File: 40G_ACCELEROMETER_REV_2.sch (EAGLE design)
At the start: 25 parts, among them IC1 3.3V_LDO, IC2 X_BUFFER, IC3 Y_BUFFER, IC4 Z_BUFFER

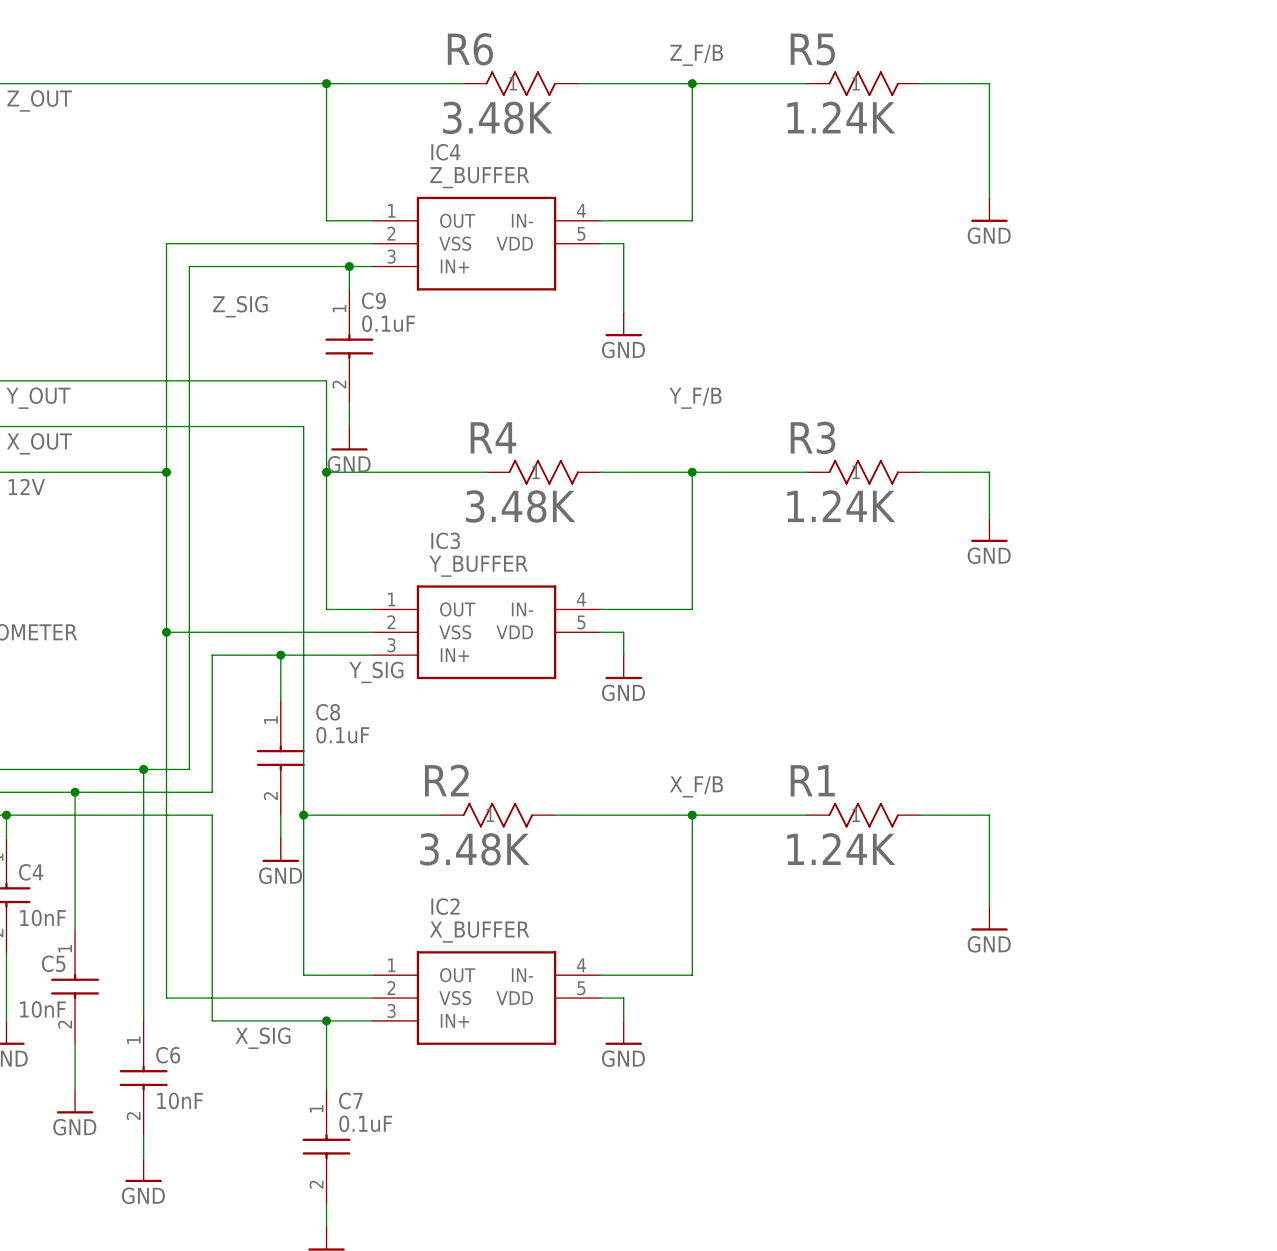
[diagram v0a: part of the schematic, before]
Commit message: New revision of board layout and fixed power connections to buffers in schematic.
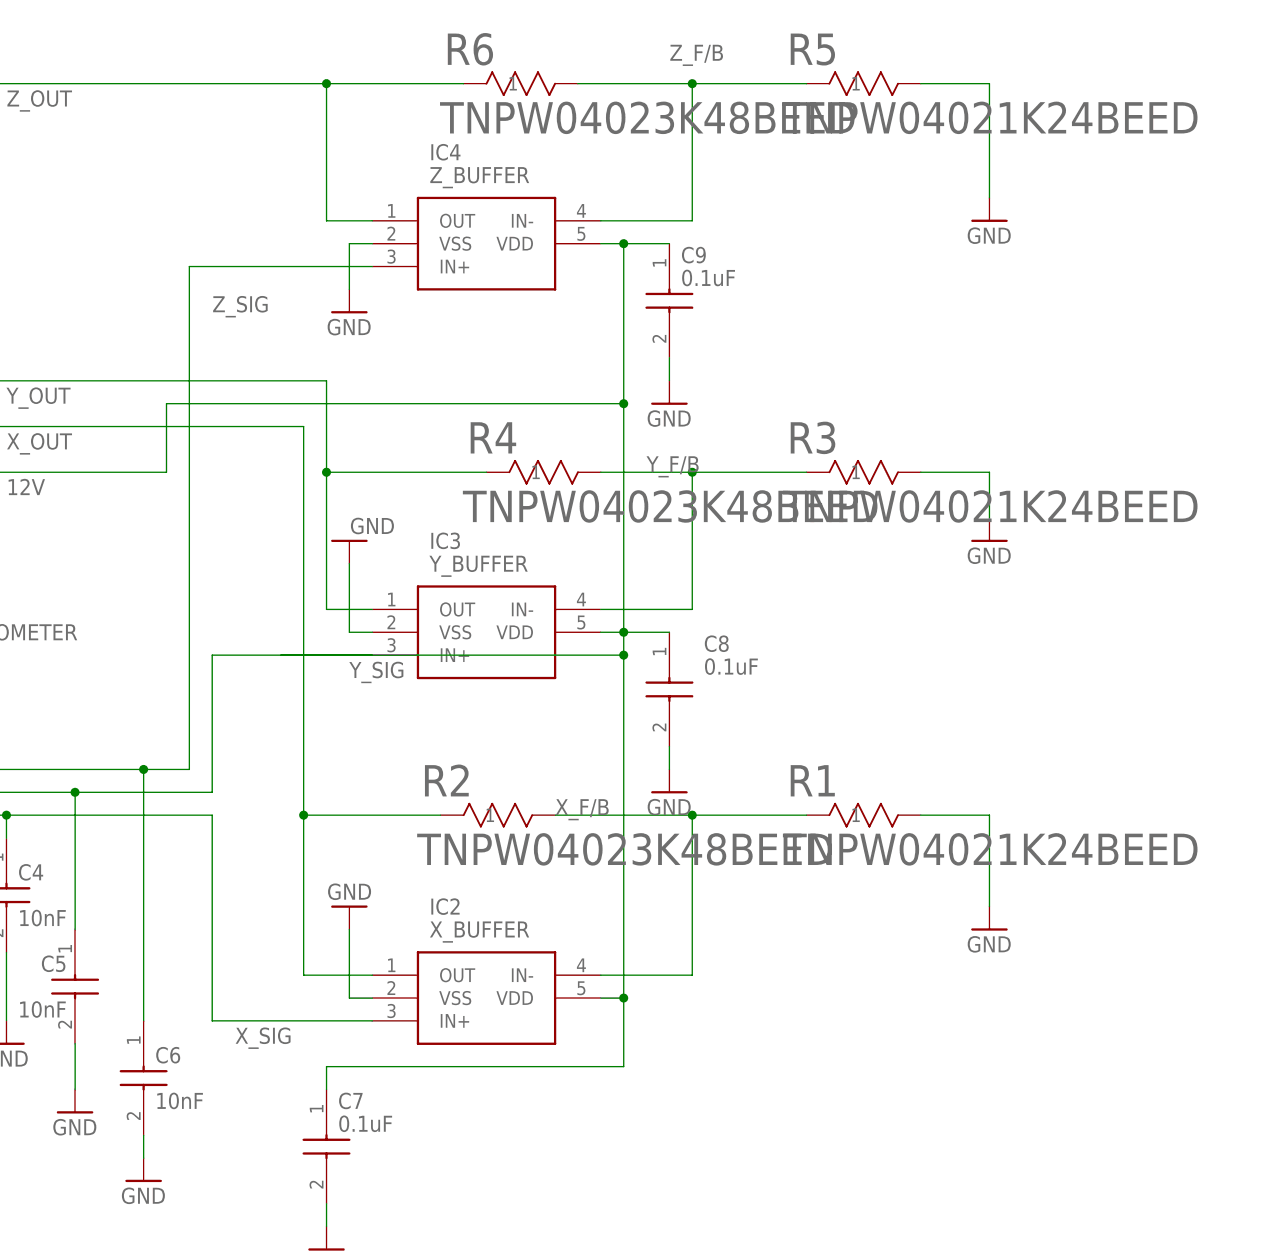
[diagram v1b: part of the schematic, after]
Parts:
- R1, R3, R5: value 1.24K -> TNPW04021K24BEED
- R2, R4, R6: value 3.48K -> TNPW04023K48BEED
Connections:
- net 12V: now also C7.1, C8.1, C9.1, IC2.VDD, IC3.VDD, IC4.VDD; no longer IC2.VSS, IC3.VSS, IC4.VSS
- net GND: now also IC2.VSS, IC3.VSS, IC4.VSS; no longer IC2.VDD, IC3.VDD, IC4.VDD
- net X_SIG: no longer C7.1
- net Y_SIG: no longer C8.1
- net Z_SIG: no longer C9.1
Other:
- moved on the sheet: C8, C9

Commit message: New layout for PCB board. Added diodes to main board pins. Ground stitching vias added. Ready for final review.
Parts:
- added D1, D2, D3, D4, D5: PTVS12VS1UR,115, SamacSys_Parts:PTVS12VS1UR,115
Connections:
- net 12V: now also D1.K
- net GND: now also D1.A, D2.A, D3.A, D4.A, D5.A, D5.K
- net X_OUT: now also D2.K
- net Y_OUT: now also D3.K
- net Z_OUT: now also D4.K
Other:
- moved on the sheet: 12V, C8, C9, GND, R1, R2, X_OUT, Y_OUT, Z_OUT

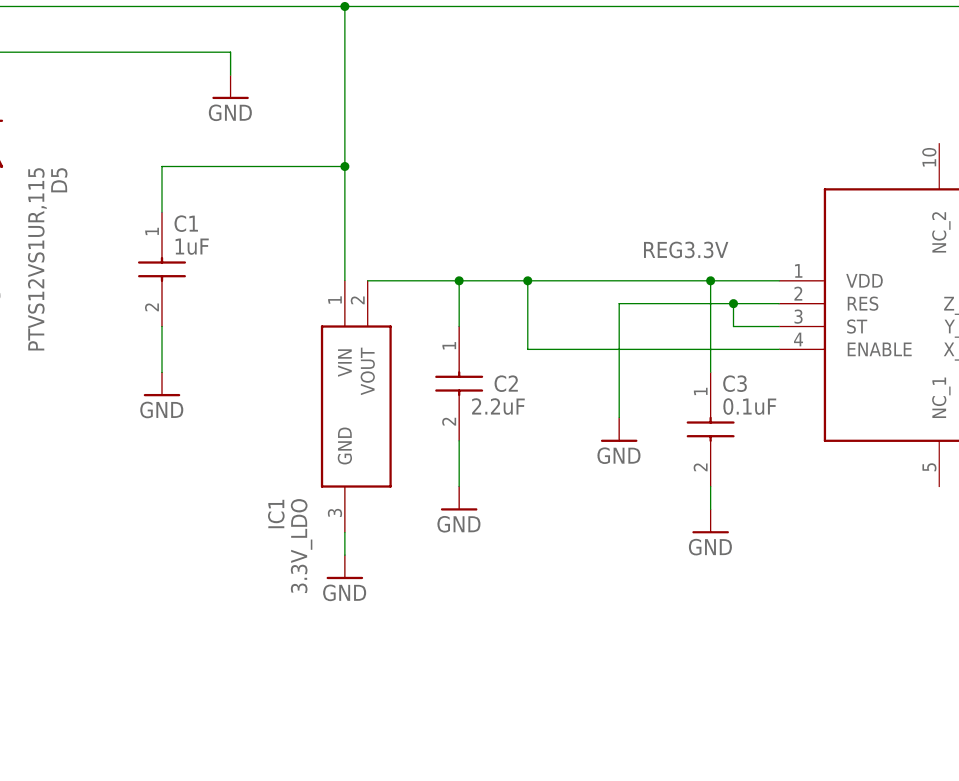
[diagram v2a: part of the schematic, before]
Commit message: Changed LDO input cap and LDO to parts that are in stock.
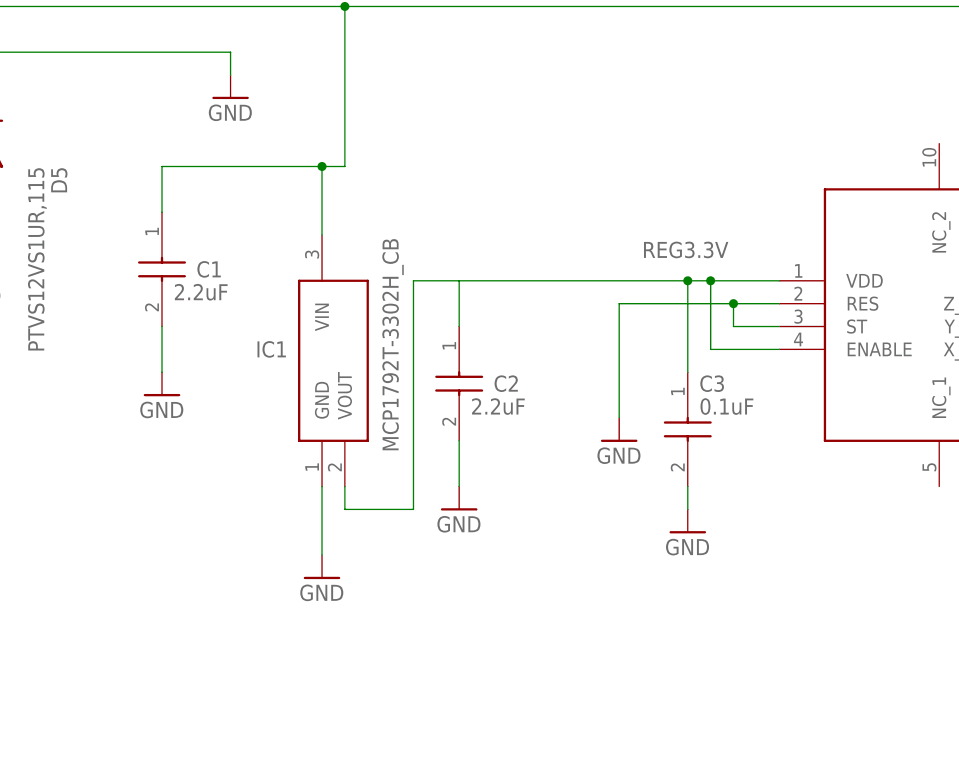
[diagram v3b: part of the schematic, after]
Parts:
- C1: value 1uF -> 2.2uF; device SamacSys_Parts:CGA3E1X7R1V105K080AE -> SamacSys_Parts:CGA3E1X7R0J225K080AC
- IC1: value 3.3V_LDO -> MCP1792T-3302H_CB; device SamacSys_Parts:AP7384-33SA-7 -> SamacSys_Parts:MCP1792T-3302H_CB
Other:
- moved on the sheet: C3, IC1
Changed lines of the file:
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@@
 <parts>
 <part name="AC1" library="SamacSys_Parts" deviceset="KX220-1072" device="" value="ACCELEROMETER"/>
-<part name="IC1" library="SamacSys_Parts" deviceset="AP7384-33SA-7" device="" value="3.3V_LDO"/>
 <part name="IC2" library="SamacSys_Parts" deviceset="NCS21911SN2T1G" device="" value="X_BUFFER"/>
 <part name="IC3" library="SamacSys_Parts" deviceset="NCS21911SN2T1G" device="" value="Y_BUFFER"/>
@@
 <part name="GND9" library="supply1" library_urn="urn:adsk.eagle:library:371" deviceset="GND" device=""/>
 <part name="GND10" library="supply1" library_urn="urn:adsk.eagle:library:371" deviceset="GND" device=""/>
-<part name="C1" library="SamacSys_Parts" deviceset="CGA3E1X7R1V105K080AE" device="" value="1uF"/>
 <part name="GND11" library="supply1" library_urn="urn:adsk.eagle:library:371" deviceset="GND" device=""/>
 <part name="C7" library="SamacSys_Parts" deviceset="CGA3E2X7R1H104K080AE" device="" value="0.1uF"/>
@@
 <part name="GND23" library="supply1" library_urn="urn:adsk.eagle:library:371" deviceset="GND" device=""/>
 <part name="GND24" library="supply1" library_urn="urn:adsk.eagle:library:371" deviceset="GND" device=""/>
+<part name="C1" library="SamacSys_Parts" deviceset="CGA3E1X7R0J225K080AC" device="" value="2.2uF"/>
+<part name="IC1" library="SamacSys_Parts" deviceset="MCP1792T-3302H_CB" device=""/>
 </parts>
 <sheets>
@@
 <attribute name="VALUE" x="97.79" y="63.5" size="1.778" layer="96" align="center-left"/>
 </instance>
-<instance part="IC1" gate="G$1" x="17.78" y="50.8" smashed="yes" rot="MR270">
-<attribute name="NAME" x="10.16" y="26.67" size="1.778" layer="95" rot="MR270" align="center-left"/>
-<attribute name="VALUE" x="12.7" y="26.67" size="1.778" layer="96" rot="MR270" align="center-left"/>
-</instance>
 <instance part="IC2" gate="G$1" x="149.86" y="25.4" smashed="yes">
 <attribute name="NAME" x="156.21" y="33.02" size="1.778" layer="95" align="center-left"/>
@@
 <attribute name="VALUE" x="215.9" y="27.94" size="1.778" layer="96"/>
 </instance>
-<instance part="GND6" gate="1" x="17.78" y="17.78" smashed="yes">
-<attribute name="VALUE" x="15.24" y="15.24" size="1.778" layer="96"/>
+<instance part="GND6" gate="1" x="15.24" y="17.78" smashed="yes">
+<attribute name="VALUE" x="12.7" y="15.24" size="1.778" layer="96"/>
 </instance>
 <instance part="C2" gate="G$1" x="30.48" y="45.72" smashed="yes" rot="R270">
@@
 <attribute name="VALUE" x="121.92" y="0" size="1.778" layer="96"/>
 </instance>
-<instance part="C1" gate="G$1" x="-2.54" y="58.42" smashed="yes" rot="R270">
-<attribute name="NAME" x="-1.27" y="57.15" size="1.778" layer="95" align="center-left"/>
-<attribute name="VALUE" x="-1.27" y="54.61" size="1.778" layer="96" align="center-left"/>
-</instance>
 <instance part="GND11" gate="1" x="-2.54" y="38.1" smashed="yes">
 <attribute name="VALUE" x="-5.08" y="35.56" size="1.778" layer="96"/>
@@
 <attribute name="VALUE" x="142.24" y="-7.62" size="1.778" layer="96"/>
 </instance>
-<instance part="C3" gate="G$1" x="58.42" y="40.64" smashed="yes" rot="R270">
-<attribute name="NAME" x="59.69" y="39.37" size="1.778" layer="95" align="center-left"/>
-<attribute name="VALUE" x="59.69" y="36.83" size="1.778" layer="96" align="center-left"/>
-</instance>
-<instance part="GND18" gate="1" x="58.42" y="22.86" smashed="yes">
-<attribute name="VALUE" x="55.88" y="20.32" size="1.778" layer="96"/>
+<instance part="C3" gate="G$1" x="55.88" y="40.64" smashed="yes" rot="R270">
+<attribute name="NAME" x="57.15" y="39.37" size="1.778" layer="95" align="center-left"/>
+<attribute name="VALUE" x="57.15" y="36.83" size="1.778" layer="96" align="center-left"/>
+</instance>
+<instance part="GND18" gate="1" x="55.88" y="22.86" smashed="yes">
+<attribute name="VALUE" x="53.34" y="20.32" size="1.778" layer="96"/>
 </instance>
 <instance part="GND19" gate="1" x="5.08" y="71.12" smashed="yes">
@@
 <attribute name="VALUE" x="-25.4" y="48.26" size="1.778" layer="96"/>
 </instance>
+<instance part="C1" gate="G$1" x="-2.54" y="58.42" smashed="yes" rot="R270">
+<attribute name="NAME" x="1.27" y="52.07" size="1.778" layer="95" align="center-left"/>
+<attribute name="VALUE" x="-1.27" y="49.53" size="1.778" layer="96" align="center-left"/>
+</instance>
+<instance part="IC1" gate="G$1" x="15.24" y="27.94" smashed="yes" rot="R90">
+<attribute name="NAME" x="11.43" y="43.18" size="1.778" layer="95" rot="R180" align="center-left"/>
+<attribute name="VALUE" x="22.86" y="31.75" size="1.778" layer="96" rot="R90" align="center-left"/>
+</instance>
 </instances>
 <busses>
@@
 <segment>
 <pinref part="AC1" gate="G$1" pin="VDD"/>
+<wire x1="30.48" y1="50.8" x2="55.88" y2="50.8" width="0.1524" layer="91"/>
+<wire x1="55.88" y1="50.8" x2="58.42" y2="50.8" width="0.1524" layer="91"/>
+<label x="50.8" y="53.34" size="1.778" layer="95"/>
+<pinref part="C2" gate="G$1" pin="1"/>
+<pinref part="C3" gate="G$1" pin="1"/>
+<wire x1="58.42" y1="50.8" x2="66.04" y2="50.8" width="0.1524" layer="91"/>
+<wire x1="55.88" y1="40.64" x2="55.88" y2="50.8" width="0.1524" layer="91"/>
+<junction x="55.88" y="50.8"/>
+<pinref part="IC1" gate="G$1" pin="VOUT"/>
+<wire x1="17.78" y1="27.94" x2="17.78" y2="25.4" width="0.1524" layer="91"/>
+<wire x1="17.78" y1="25.4" x2="25.4" y2="25.4" width="0.1524" layer="91"/>
+<wire x1="25.4" y1="25.4" x2="25.4" y2="50.8" width="0.1524" layer="91"/>
+<wire x1="25.4" y1="50.8" x2="30.48" y2="50.8" width="0.1524" layer="91"/>
+<wire x1="30.48" y1="50.8" x2="30.48" y2="45.72" width="0.1524" layer="91"/>
 <pinref part="AC1" gate="G$1" pin="ENABLE"/>
-<wire x1="38.1" y1="50.8" x2="58.42" y2="50.8" width="0.1524" layer="91"/>
-<wire x1="58.42" y1="50.8" x2="66.04" y2="50.8" width="0.1524" layer="91"/>
-<wire x1="38.1" y1="50.8" x2="38.1" y2="43.18" width="0.1524" layer="91"/>
-<wire x1="38.1" y1="43.18" x2="66.04" y2="43.18" width="0.1524" layer="91"/>
-<label x="50.8" y="53.34" size="1.778" layer="95"/>
-<pinref part="IC1" gate="G$1" pin="VOUT"/>
-<wire x1="20.32" y1="50.8" x2="30.48" y2="50.8" width="0.1524" layer="91"/>
-<junction x="38.1" y="50.8"/>
-<pinref part="C2" gate="G$1" pin="1"/>
-<wire x1="30.48" y1="50.8" x2="38.1" y2="50.8" width="0.1524" layer="91"/>
-<wire x1="30.48" y1="45.72" x2="30.48" y2="50.8" width="0.1524" layer="91"/>
-<junction x="30.48" y="50.8"/>
-<pinref part="C3" gate="G$1" pin="1"/>
-<wire x1="58.42" y1="40.64" x2="58.42" y2="50.8" width="0.1524" layer="91"/>
+<wire x1="66.04" y1="43.18" x2="58.42" y2="43.18" width="0.1524" layer="91"/>
+<wire x1="58.42" y1="43.18" x2="58.42" y2="50.8" width="0.1524" layer="91"/>
 <junction x="58.42" y="50.8"/>
 </segment>
@@
 </segment>
 <segment>
-<pinref part="GND6" gate="1" pin="GND"/>
-<pinref part="IC1" gate="G$1" pin="GND"/>
-<wire x1="17.78" y1="20.32" x2="17.78" y2="22.86" width="0.1524" layer="91"/>
-</segment>
-<segment>
 <pinref part="C2" gate="G$1" pin="2"/>
 <pinref part="GND7" gate="1" pin="GND"/>
@@
 </segment>
 <segment>
-<pinref part="C1" gate="G$1" pin="2"/>
 <pinref part="GND11" gate="1" pin="GND"/>
 <wire x1="-2.54" y1="45.72" x2="-2.54" y2="40.64" width="0.1524" layer="91"/>
+<pinref part="C1" gate="G$1" pin="2"/>
 </segment>
 <segment>
@@
 <pinref part="C3" gate="G$1" pin="2"/>
 <pinref part="GND18" gate="1" pin="GND"/>
-<wire x1="58.42" y1="27.94" x2="58.42" y2="25.4" width="0.1524" layer="91"/>
+<wire x1="55.88" y1="27.94" x2="55.88" y2="25.4" width="0.1524" layer="91"/>
 </segment>
 <segment>
@@
 <pinref part="GND23" gate="1" pin="GND"/>
 <wire x1="7.62" y1="144.78" x2="7.62" y2="149.86" width="0.1524" layer="91"/>
+</segment>
+<segment>
+<pinref part="IC1" gate="G$1" pin="GND"/>
+<pinref part="GND6" gate="1" pin="GND"/>
+<wire x1="15.24" y1="27.94" x2="15.24" y2="20.32" width="0.1524" layer="91"/>
 </segment>
 </net>
@@
 <net name="12V" class="0">
 <segment>
-<pinref part="IC1" gate="G$1" pin="VIN"/>
-<wire x1="17.78" y1="50.8" x2="17.78" y2="63.5" width="0.1524" layer="91"/>
 <wire x1="17.78" y1="63.5" x2="17.78" y2="81.28" width="0.1524" layer="91"/>
 <wire x1="17.78" y1="81.28" x2="-50.8" y2="81.28" width="0.1524" layer="91"/>
@@
 <junction x="17.78" y="81.28"/>
 <label x="109.22" y="78.74" size="1.778" layer="95"/>
-<pinref part="C1" gate="G$1" pin="1"/>
 <wire x1="-2.54" y1="58.42" x2="-2.54" y2="63.5" width="0.1524" layer="91"/>
-<wire x1="-2.54" y1="63.5" x2="17.78" y2="63.5" width="0.1524" layer="91"/>
-<junction x="17.78" y="63.5"/>
+<wire x1="-2.54" y1="63.5" x2="15.24" y2="63.5" width="0.1524" layer="91"/>
 <pinref part="12V" gate="1" pin="P"/>
+<wire x1="15.24" y1="63.5" x2="17.78" y2="63.5" width="0.1524" layer="91"/>
 <wire x1="127" y1="81.28" x2="127" y2="88.9" width="0.1524" layer="91"/>
 <wire x1="127" y1="88.9" x2="177.8" y2="88.9" width="0.1524" layer="91"/>
@@
 <wire x1="-50.8" y1="83.82" x2="-50.8" y2="81.28" width="0.1524" layer="91"/>
 <junction x="-50.8" y="81.28"/>
+<pinref part="C1" gate="G$1" pin="1"/>
+<pinref part="IC1" gate="G$1" pin="VIN"/>
+<wire x1="15.24" y1="63.5" x2="15.24" y2="55.88" width="0.1524" layer="91"/>
+<junction x="15.24" y="63.5"/>
 </segment>
 </net>
